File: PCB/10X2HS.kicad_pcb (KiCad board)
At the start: 2 copper layers, 161.5 x 86.5 mm, 30 parts, among them SW01 SW, SW02 SW, SW03 SW, SW04 SW, SW05 SW, SW06 SW, SW07 SW, SW08 SW, SW09 SW, SW10 SW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

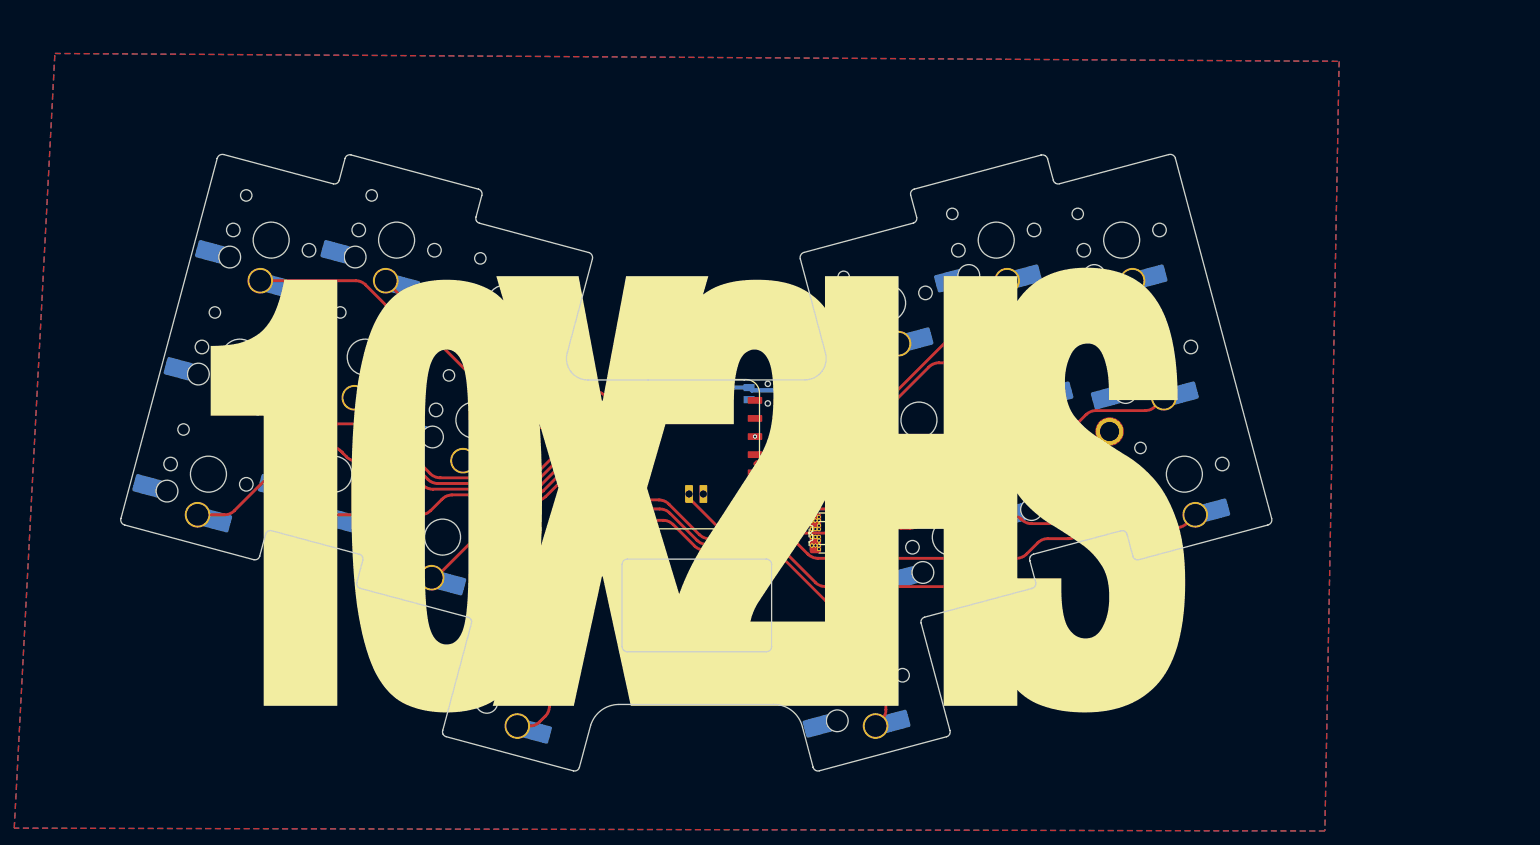
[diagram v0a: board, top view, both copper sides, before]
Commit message: changed to nonplus xiao, add direct battery pads
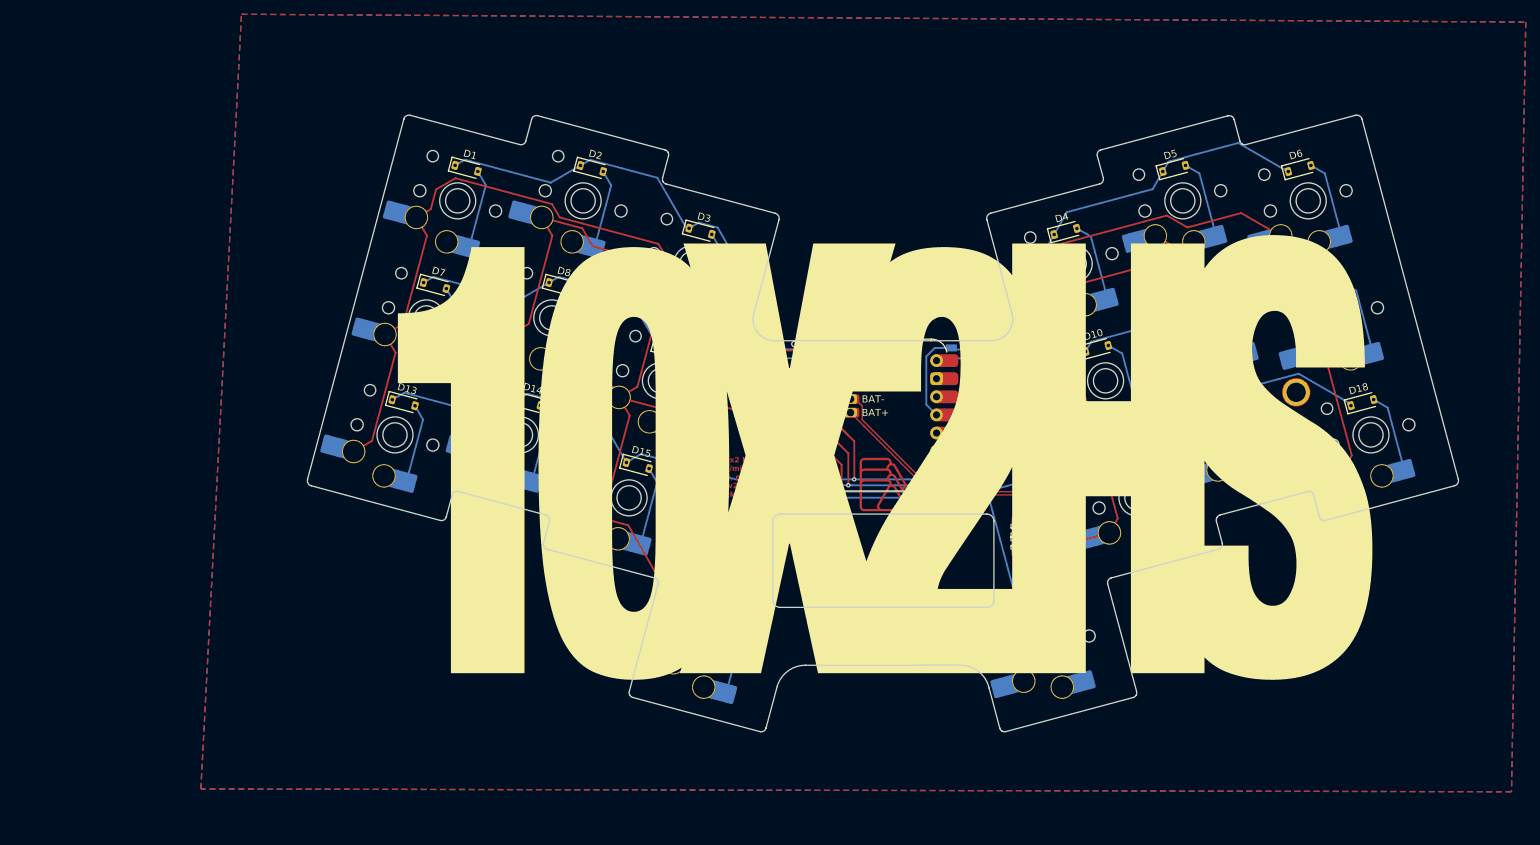
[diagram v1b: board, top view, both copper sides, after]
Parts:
- removed SW01, SW02, SW03, SW04, SW05, SW06, SW07, SW08, SW09: SW, PCM_Switch_Keyboard_Hotswap_Kailh:SW_Hotswap_Kailh_Choc_V1V2_Plated_1.00u reversible offset whoops
- removed U2: Seeeduino Xiao nRF52840 Plus, xiao nrf52840 plus:XIAO-nRF52840-Plus-SMD with non stupid pads
- added D1: 1n4148, zackforbing:D_SOD-123, F.Cu at (96.1, 55.8)
- added D10: 1n4148, zackforbing:D_SOD-123, F.Cu at (184.6, 81.1)
- added D11: 1n4148, zackforbing:D_SOD-123, F.Cu at (199.8, 72.2)
- added D12: 1n4148, zackforbing:D_SOD-123, F.Cu at (217.4, 72.2)
- added D13: 1n4148, zackforbing:D_SOD-123, F.Cu at (87.3, 88.7)
- added D14: 1n4148, zackforbing:D_SOD-123, F.Cu at (104.9, 88.6)
- added D15: 1n4148, zackforbing:D_SOD-123, F.Cu at (120.2, 97.5)
- added D16: 1n4148, zackforbing:D_SOD-123, F.Cu at (189.0, 97.5)
- added D17: 1n4148, zackforbing:D_SOD-123, F.Cu at (204.2, 88.6)
- added D18: 1n4148, zackforbing:D_SOD-123, F.Cu at (221.8, 88.7)
- added D19: 1n4148, zackforbing:D_SOD-123, F.Cu at (132.2, 118.3)
- added D2: 1n4148, zackforbing:D_SOD-123, F.Cu at (113.7, 55.8)
- added D20: 1n4148, zackforbing:D_SOD-123, F.Cu at (177.0, 118.3)
- added D3: 1n4148, zackforbing:D_SOD-123, F.Cu at (129.0, 64.6)
- added D4: 1n4148, zackforbing:D_SOD-123, F.Cu at (180.2, 64.6)
- added D5: 1n4148, zackforbing:D_SOD-123, F.Cu at (195.4, 55.8)
- added D6: 1n4148, zackforbing:D_SOD-123, F.Cu at (213.0, 55.8)
- added D7: 1n4148, zackforbing:D_SOD-123, F.Cu at (91.7, 72.2)
- added D8: 1n4148, zackforbing:D_SOD-123, F.Cu at (109.3, 72.2)
- added D9: 1n4148, zackforbing:D_SOD-123, F.Cu at (124.5, 81.1)
- added REF**: ha ha ha logo, zackforbing:ha ha ha logo, F.Cu at (154.6, 100.1)
- added REF**: PinHeader_2x01_P2.00mm_Vertical, Connector_PinHeader_2.00mm:PinHeader_2x01_P2.00mm_Vertical, F.Cu at (177.1, 112.9)
- added SW1: MX_SW_solder, zackforbing:choc hs v1v2 led, B.Cu at (94.9, 60.3)
- added SW2: MX_SW_solder, zackforbing:choc hs v1v2 led, B.Cu at (112.5, 60.3)
- added SW22: SW_Push, Button_Switch_SMD:Panasonic_EVQPUL_EVQPUC, B.Cu at (166.8, 81.8)
- added SW3: MX_SW_solder, zackforbing:choc hs v1v2 led, B.Cu at (127.7, 69.2)
- added SW4: MX_SW_solder, zackforbing:choc hs v1v2 led, B.Cu at (181.4, 69.2)
- added SW5: MX_SW_solder, zackforbing:choc hs v1v2 led, B.Cu at (196.6, 60.3)
- added SW6: MX_SW_solder, zackforbing:choc hs v1v2 led, B.Cu at (214.2, 60.3)
- added SW7: MX_SW_solder, zackforbing:choc hs v1v2 led, B.Cu at (90.5, 76.8)
- added SW8: MX_SW_solder, zackforbing:choc hs v1v2 led, B.Cu at (108.1, 76.8)
- added SW9: MX_SW_solder, zackforbing:choc hs v1v2 led, B.Cu at (123.3, 85.6)
- added U1: Seeeduino Xiao nRF52840, PCM_marbastlib-xp-promicroish:Xiao_nRF52840_ACH, F.Cu at (154.5, 90.4)
- SW10, SW11, SW12, SW13, SW14, SW15, SW16, SW17, SW18, SW19, SW20: value SW -> MX_SW_solder; footprint PCM_Switch_Keyboard_Hotswap_Kailh:SW_Hotswap_Kailh_Choc_V1V2_Plated_1.00u reversible offset whoops -> zackforbing:choc hs v1v2 led
- moved H05 34.9 mm to (137.1, 93.5)
- moved REF** 28.3 mm to (175.2, 108.1)
- moved SW14 27.5 mm to (103.7, 93.2)
- moved SW13 27.5 mm to (86.1, 93.2)
- moved SW15 27.5 mm to (118.9, 102.0)
- moved SW19 27.5 mm to (131.0, 122.8)
- moved H07 26.8 mm to (100.8, 70.7)
- moved H03 26.8 mm to (154.6, 121.1)
- moved H01 26.8 mm to (212.5, 87.2)
- moved H02 26.8 mm to (208.2, 70.6)
- moved H06 26.8 mm to (96.5, 87.2)
- moved SW18 26.0 mm to (223.0, 93.2)
- moved SW12 26.0 mm to (218.6, 76.8)
- moved SW20 26.0 mm to (178.2, 122.8)
- moved SW10 26.0 mm to (185.8, 85.6)
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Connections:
- REF** pad 2: GND -> BAT-
- SW10 pad 1: SW10 -> COL3
- SW10 pad 2: GND -> Net-(D10-A)
- SW11 pad 1: SW11 -> COL4
- SW11 pad 2: GND -> Net-(D11-A)
- SW12 pad 1: SW12 -> COL5
- SW12 pad 2: GND -> Net-(D12-A)
- SW13 pad 1: SW13 -> COL0
- SW13 pad 2: GND -> Net-(D13-A)
- SW14 pad 1: SW14 -> COL1
- SW14 pad 2: GND -> Net-(D14-A)
- SW15 pad 1: SW15 -> COL2
- SW15 pad 2: GND -> Net-(D15-A)
- SW16 pad 1: SW16 -> COL3
- SW16 pad 2: GND -> Net-(D16-A)
- SW17 pad 1: SW17 -> COL4
- SW17 pad 2: GND -> Net-(D17-A)
- SW18 pad 1: SW18 -> COL5
- SW18 pad 2: GND -> Net-(D18-A)
- SW19 pad 1: SW19 -> COL2
- SW19 pad 2: GND -> Net-(D19-A)
- SW20 pad 1: SW20 -> COL3
- SW20 pad 2: GND -> Net-(D20-A)
- SW21 pad 1: RST -> GND
- SW21 pad 2: GND -> RST
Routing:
- net ROW0: track 0.00 -> 196.0 mm, vias 0 -> 1
- net ROW1: track 0.00 -> 169.1 mm, vias 0 -> 1
- net ROW2: track 0.00 -> 155.9 mm, vias 0 -> 1
- net COL0: track 0.00 -> 108.9 mm
- net COL5: track 0.00 -> 103.6 mm
- net COL2: track 0.00 -> 95.0 mm
- net COL1: track 0.00 -> 86.2 mm
- net COL4: track 0.00 -> 84.6 mm
- net COL3: track 0.00 -> 84.4 mm
- net SW18: track 83.7 -> 0.00 mm
- net ROW3: track 0.00 -> 73.8 mm, vias 0 -> 1
- net SW13: track 69.3 -> 0.00 mm
- net SW06: track 63.7 -> 0.00 mm
- net SW07: track 63.4 -> 0.00 mm
- net SW12: track 62.4 -> 0.00 mm
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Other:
- outline, holes or cut-outs redrawn
- board text added: "based on 10x2 by miketronic github.com/miketronic/10x2 hotswapped, nerfed, dioded, and v2ed by ha ha ha github.com/zackforbing/10x2HS"
- board text removed: "based on 10x2 by miketronic https://github.com/miketronic/10x2 hotswapped, nerfed, snipped, and v2ed by ha ha ha https://github.com/zackforbing/10x2HS"
